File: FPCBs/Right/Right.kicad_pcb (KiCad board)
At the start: 2 copper layers, 74.2 x 89.3 mm, 24 parts, among them J1 PCB, J2 LEDs, J3 LEDs, J5 2nd Focus+Shutter, J6 Conn_01x03_Pin, SW1 Mode Dial, SW2 ON/OFF, SW3 Focus+Shutter, SW4 Focus+Shutter, U1 SG-105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

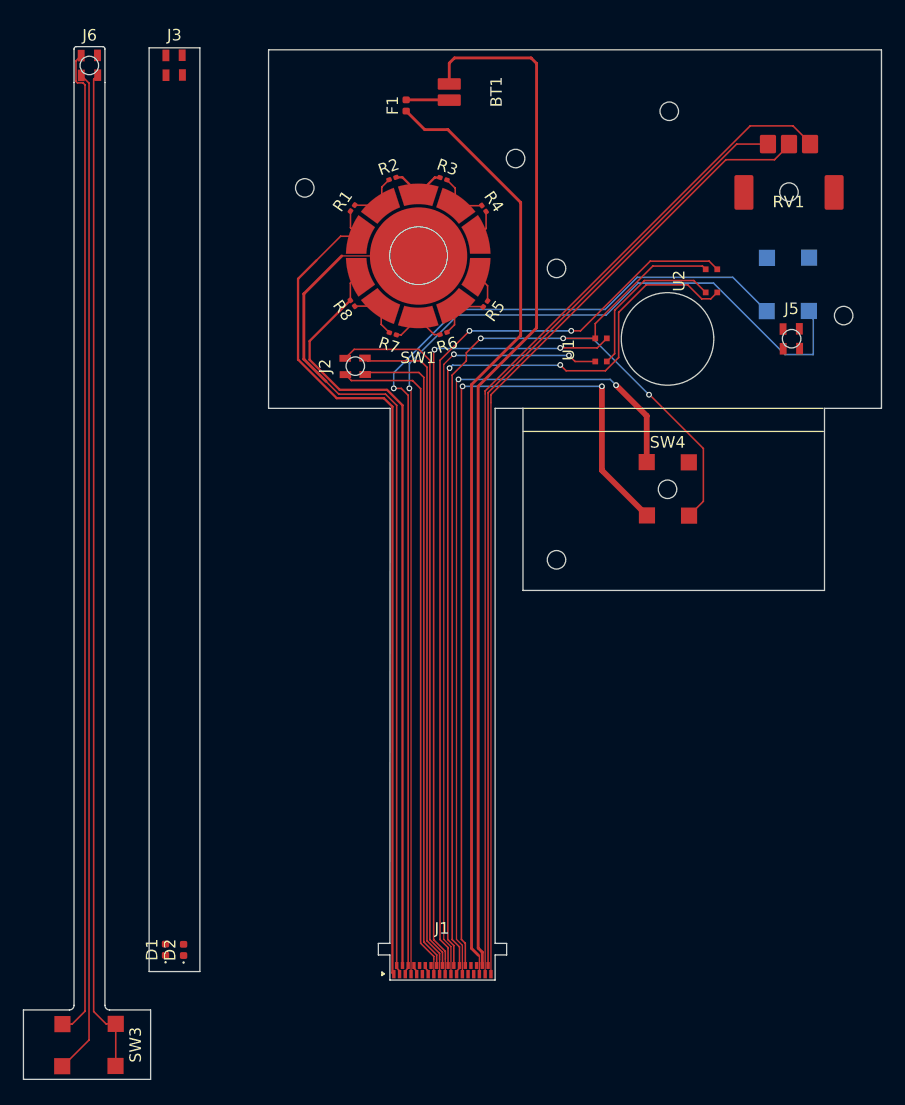
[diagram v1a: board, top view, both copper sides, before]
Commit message: Fix 4 pins connector
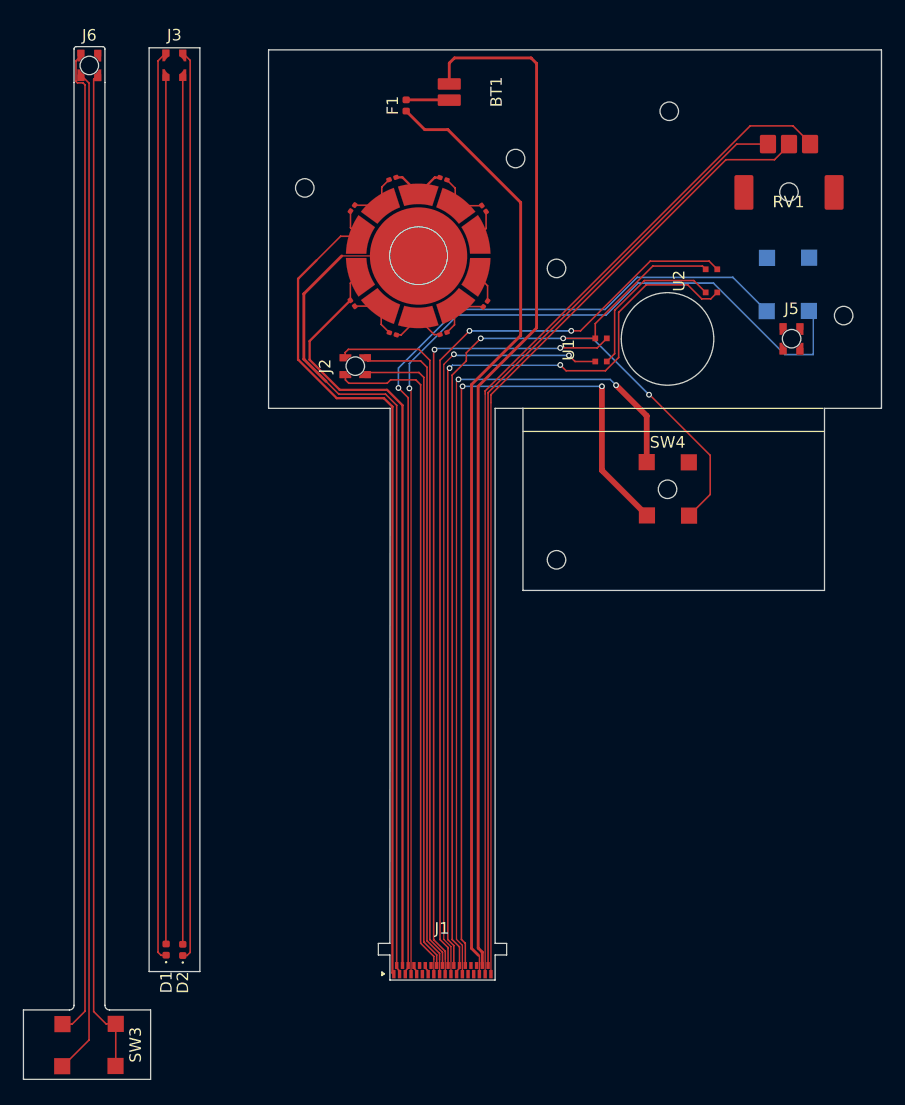
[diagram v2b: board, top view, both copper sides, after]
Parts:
- moved D2 0.07 mm to (92.6, 177.8)
- moved D1 0.05 mm to (91.1, 177.8)
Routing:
- net Net-(D1-K): track 0.00 -> 78.8 mm
- net Net-(D2-K): track 0.00 -> 78.8 mm
- net Net-(D2-A): track 0.00 -> 75.0 mm
- net Net-(D1-A): track 0.00 -> 74.9 mm
- net Net-(J1-Pin_5): track 89.7 -> 89.0 mm
- net Net-(J1-Pin_15): track 58.1 -> 58.8 mm

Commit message: Move leds to Right board
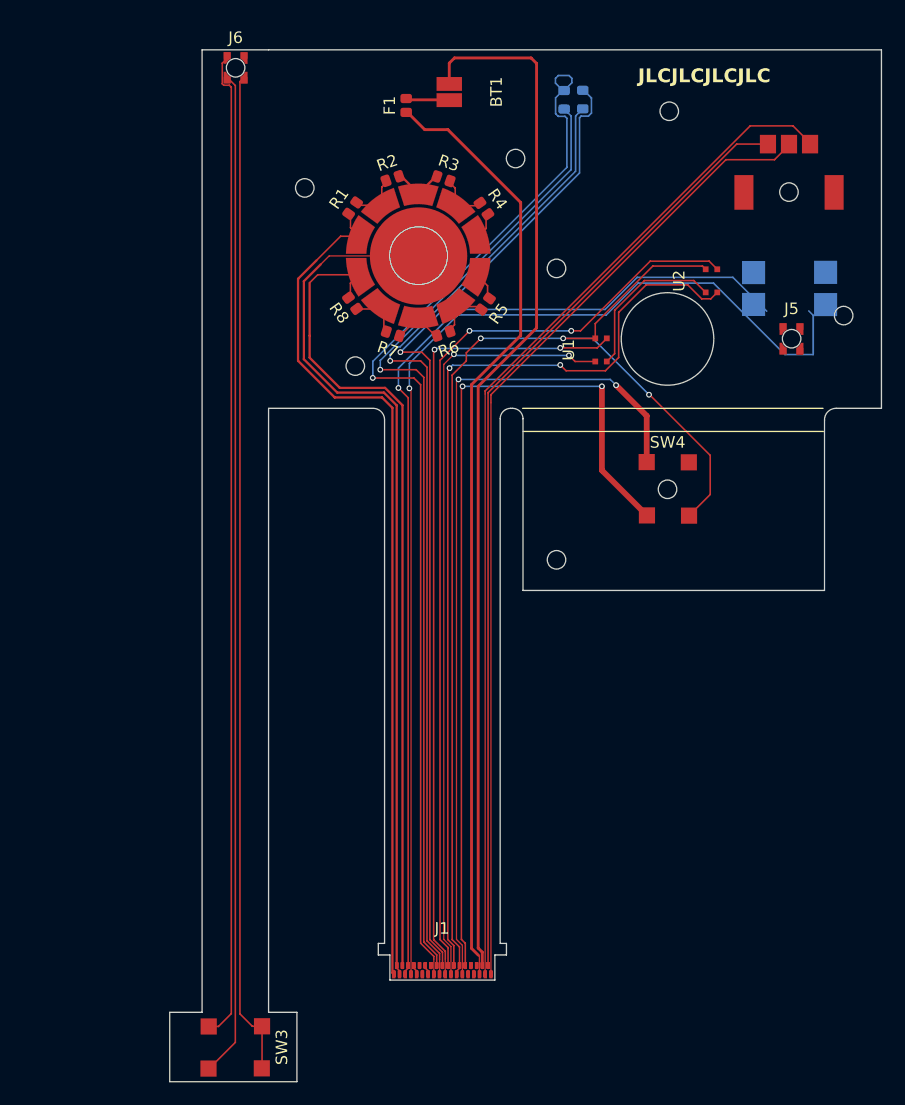
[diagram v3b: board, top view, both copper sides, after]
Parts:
- removed J2, J3: LEDs, Leica-G9ii:Connector-4Pins
- D1, D2: footprint LED_SMD:LED_0402_1005Metric -> Leica-G9ii:LED; moved to B.Cu
- F1: footprint Fuse:Fuse_0402_1005Metric -> Leica-G9ii:R_2x1mm
- J1: footprint Leica-G9ii:FPC-2Rows-35Pins-0.23mm -> Leica-G9ii:FPC-2Rows-35Pins-0.5mm
- R1, R2, R3, R4, R5, R6, R7, R8: footprint Resistor_SMD:R_0201_0603Metric -> Leica-G9ii:R_2x1mm
- SW2: footprint Leica-G9ii:Switch_Power -> Leica-G9ii:Switch_Detection_Bidirectional
- moved D2 81.3 mm to (127.2, 104.3), turned to -90 degrees
- moved D1 81.1 mm to (125.6, 104.3), turned to -90 degrees
- moved J6 12.7 mm to (97.2, 101.6)
- moved SW3 12.7 mm to (97.1, 186.2)
- moved SW2 2.48 mm to (145.1, 117.8)
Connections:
- J1 pad 15: Net-(J1-Pin_15) -> Net-(D1-K)
- J1 pad 16: Net-(J1-Pin_16) -> Net-(D1-A)
- J1 pad 17: Net-(J1-Pin_17) -> Net-(D2-A)
- J1 pad 18: Net-(J1-Pin_18) -> Net-(D2-K)
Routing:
- net Net-(J1-Pin_18): track 61.1 -> 0.00 mm
- net Net-(J1-Pin_15): track 58.8 -> 0.00 mm
- net Net-(J1-Pin_17): track 58.6 -> 0.00 mm
- net Net-(J1-Pin_16): track 56.6 -> 0.00 mm
- net Net-(D1-K): track 78.8 -> 92.9 mm, vias 0 -> 1
- net Net-(D2-A): track 75.0 -> 85.1 mm, vias 0 -> 1
- net Net-(D1-A): track 74.9 -> 85.0 mm, vias 0 -> 1
- net Net-(D2-K): track 78.8 -> 85.8 mm, vias 0 -> 1
- net Net-(J1-Pin_4): track 67.2 -> 71.9 mm
- net Net-(J1-Pin_2): track 72.5 -> 73.1 mm
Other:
- board size 74.2 x 89.3 mm -> 61.5 x 89.2 mm
- board text added: "JLCJLCJLCJLC"

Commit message: Add extra switch for on/off
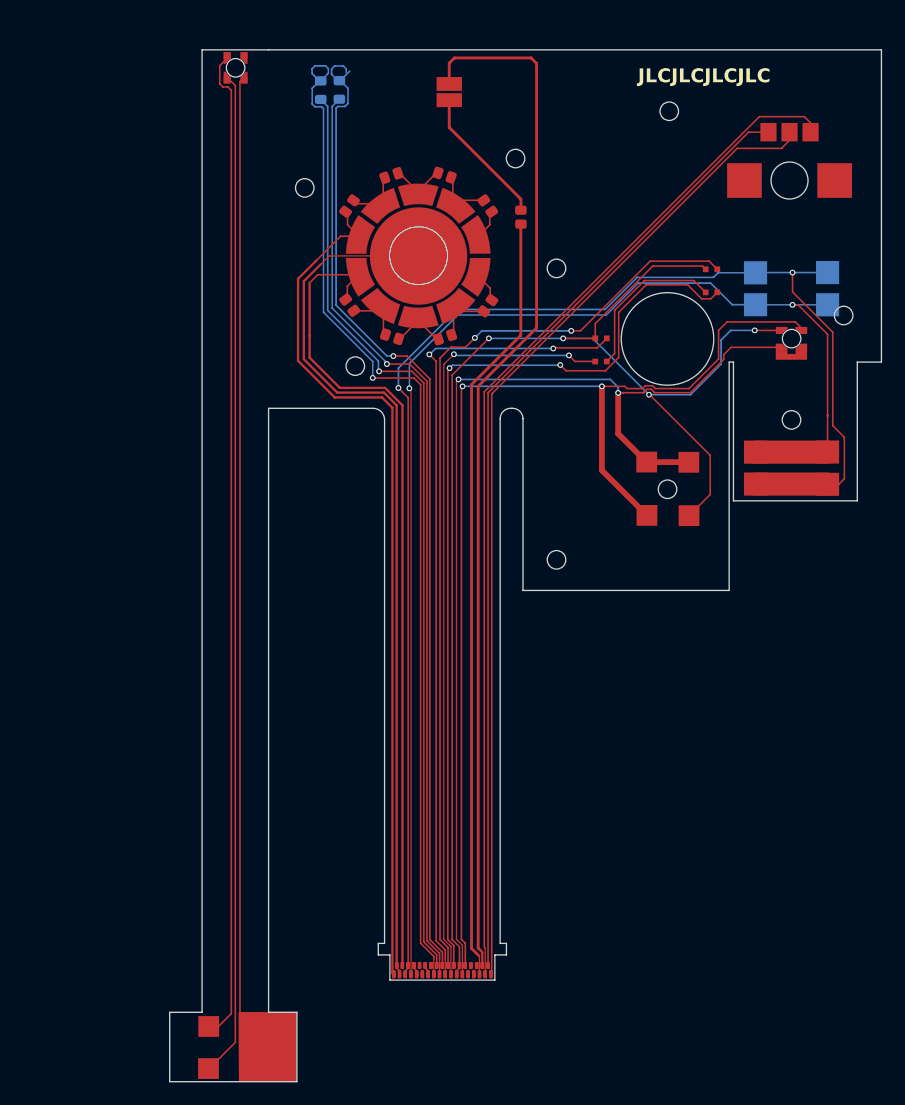
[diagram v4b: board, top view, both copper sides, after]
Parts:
- added SW6: ON/OFF, Leica-G9ii:Switch_Detection_Bidirectional, F.Cu at (145.2, 139.0)
- moved D1 21.1 mm to (104.5, 103.5)
- moved D2 21.1 mm to (106.1, 103.5)
- moved F1 13.8 mm to (121.8, 114.5)
- moved RV1 1.03 mm to (145.1, 111.3)
- moved R4 0.40 mm to (119.0, 113.5)
- moved R6 0.34 mm to (115.3, 124.8)
- moved R3 0.32 mm to (115.2, 110.8)
- moved R1 0.32 mm to (107.0, 113.5)
- moved R8 0.29 mm to (107.0, 122.1)
- moved R2 0.28 mm to (110.6, 110.9)
- moved R7 0.27 mm to (110.7, 124.8)
- moved R5 0.26 mm to (119.0, 122.1)
- moved SW2 0.17 mm to (145.2, 117.8)
- turned J5 to -90 degrees
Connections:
- SW2 pad 1: Net-(J1-Pin_7) -> Net-(J1-Pin_5)
- SW2 pad 2: Net-(J1-Pin_5) -> Net-(J1-Pin_7)
- SW2 pad 3: (no net) -> Net-(J1-Pin_7)
- SW3 pad 1: Net-(J6-Pin_1) -> Net-(J6-Pin_2)
- SW3 pad 2: Net-(J6-Pin_2) -> Net-(J6-Pin_1)
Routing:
- net Net-(J1-Pin_5): track 89.0 -> 120.8 mm, vias 1 -> 2
- net Net-(J1-Pin_26): track 75.1 -> 96.9 mm
- net Net-(J1-Pin_25): track 73.4 -> 93.1 mm
- net Net-(J1-Pin_7): track 97.2 -> 113.3 mm, vias 1 -> 2
- net Net-(J1-Pin_31): track 81.9 -> 66.9 mm
- net Net-(J1-Pin_23): track 102.1 -> 116.5 mm, vias 3 -> 4
- net Net-(BT1-+): track 3.74 -> 12.1 mm
- net Net-(D1-K): track 92.9 -> 88.5 mm
- net Net-(D1-A): track 85.0 -> 80.7 mm
- net Net-(D2-A): track 85.1 -> 80.9 mm
- net Net-(D2-K): track 85.8 -> 86.9 mm
- net Net-(J1-Pin_35): track 84.9 -> 85.7 mm
- net Net-(J1-Pin_33): track 88.7 -> 89.5 mm
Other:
- outline, holes or cut-outs redrawn

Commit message: Add copper tot he back side
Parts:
- moved U2 3.58 mm to (134.8, 120.7), turned to 90 degrees
- moved U1 1.62 mm to (130.2, 125.3)
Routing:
- net Net-(J1-Pin_20): track 80.5 -> 74.5 mm
- net Net-(J1-Pin_23): track 116.5 -> 110.6 mm
- net Net-(J1-Pin_5): track 120.8 -> 123.3 mm
- net Net-(J1-Pin_22): track 81.5 -> 83.9 mm
- net Net-(J1-Pin_19): track 70.2 -> 72.0 mm
- net Net-(U1-K): track 14.1 -> 15.8 mm
- net Net-(J1-Pin_21): track 66.7 -> 68.0 mm
- added copper zone on B.Cu, net (none)
- added copper zone on F.Cu, net Net-(J6-Pin_3)
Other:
- outline, holes or cut-outs redrawn

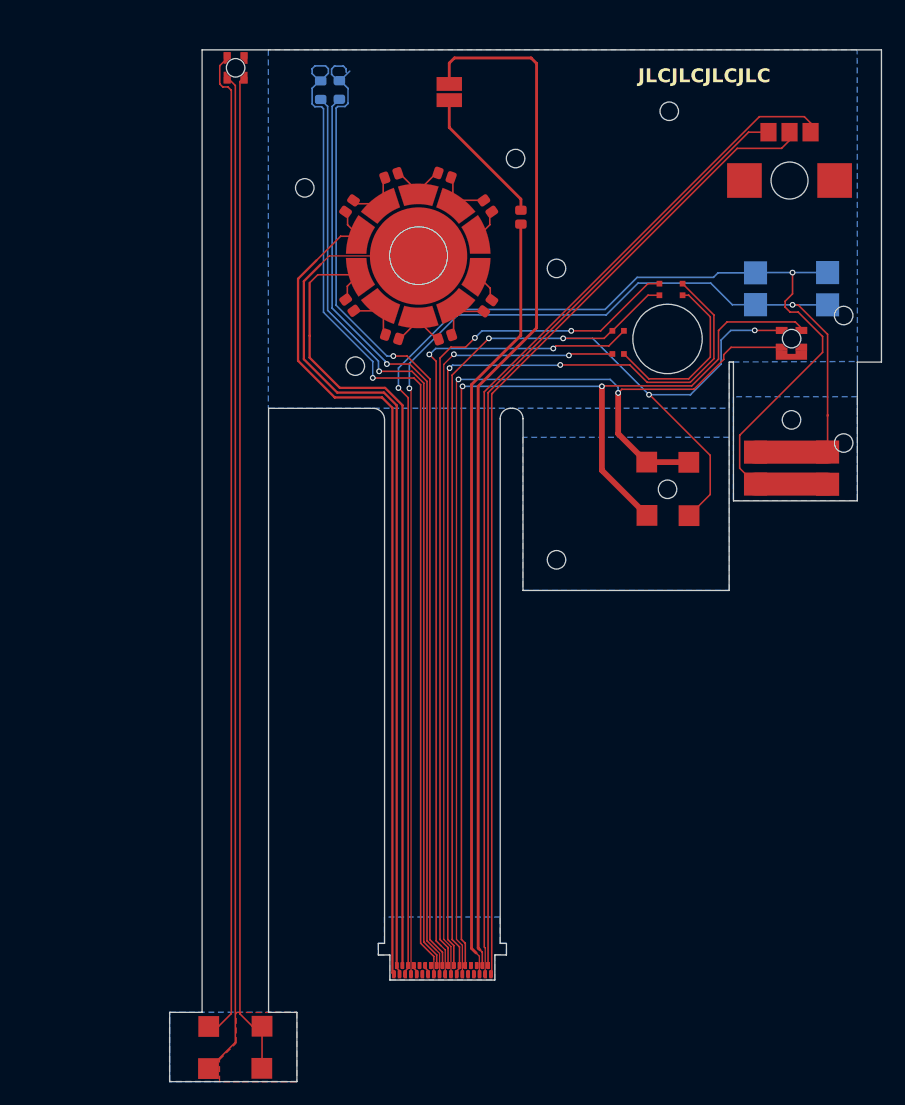
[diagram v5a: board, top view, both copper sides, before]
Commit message: Add Canon shutter footprint
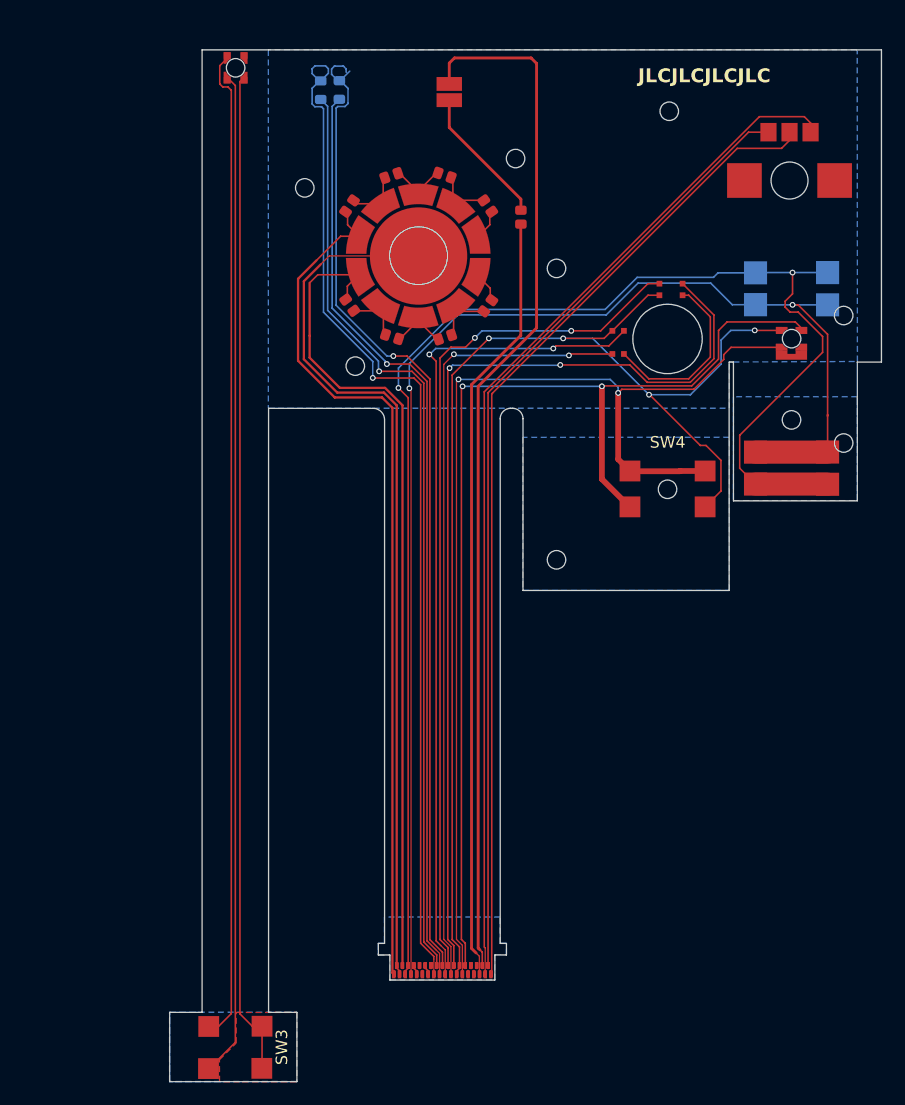
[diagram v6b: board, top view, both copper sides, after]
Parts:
- SW3: footprint Leica-G9ii:Switch_Shutter_1 -> Leica-G9ii:Switch_Shutter_Olympus
- SW4: footprint Leica-G9ii:Switch_Shutter_1 -> Leica-G9ii:Switch_Shutter_Canon
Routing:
- net Net-(J1-Pin_25): track 92.8 -> 95.8 mm
- net Net-(J1-Pin_26): track 96.6 -> 95.3 mm
